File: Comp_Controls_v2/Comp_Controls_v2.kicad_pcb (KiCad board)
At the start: 2 copper layers, 78.1 x 108.9 mm, 42 parts

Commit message: fixed DRC warnings so far
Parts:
- removed ? (x3): , 
- renumbered VectorNavInput1 to VectorNavInput
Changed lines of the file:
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@@
 			(at -0.21 -1.05 0)
 			(layer "F.SilkS")
+			(hide yes)
 			(effects
 				(font
@@
 			(at -2.13 0.04 180)
 			(layer "F.SilkS")
+			(hide yes)
 			(effects
 				(font
@@
 			(at 1.54 1.05 90)
 			(layer "F.Fab")
+			(hide yes)
 			(effects
 				(font
@@
 		(descr "9-pin D-Sub connector, straight/vertical, THT-mount, socket (female), pitch 2.77x2.84mm, distance of mounting holes 25mm, see https://disti-assets.s3.amazonaws.com/tonar/files/datasheets/16730.pdf")
 		(tags "9-pin D-Sub connector straight vertical THT socket pitch 2.77x2.84mm mounting holes distance 25mm")
-		(property "Reference" "VectorNavInput1"
-			(at -5.54 -5.89 90)
+		(property "Reference" "VectorNavInput"
+			(at -6.17 9.38 90)
 			(layer "F.SilkS")
 			(effects
@@
 			(at -2.03 -0.09 180)
 			(layer "F.SilkS")
+			(hide yes)
 			(effects
 				(font
@@
 		(embedded_fonts no)
 	)
-	(footprint ""
-		(layer "F.Cu")
-		(at 118.915 39.48)
-		(property "Reference" ""
-			(at 0 0 0)
-			(layer "F.SilkS")
-			(effects
-				(font
-					(size 1.27 1.27)
-					(thickness 0.15)
-				)
-			)
-		)
-		(property "Value" ""
-			(at 0 0 0)
-			(layer "F.Fab")
-			(effects
-				(font
-					(size 1.27 1.27)
-					(thickness 0.15)
-				)
-			)
-		)
-		(property "Datasheet" ""
-			(at 0 0 0)
-			(layer "F.Fab")
-			(hide yes)
-			(effects
-				(font
-					(size 1.27 1.27)
-					(thickness 0.15)
-				)
-			)
-		)
-		(property "Description" ""
-			(at 0 0 0)
-			(layer "F.Fab")
-			(hide yes)
-			(effects
-				(font
-					(size 1.27 1.27)
-					(thickness 0.15)
-				)
-			)
-		)
-		(pad "" np_thru_hole circle
-			(at 0 0)
-			(size 3.2 3.2)
-			(drill 3.2)
-			(layers "*.Cu" "*.Mask")
-		)
-		(embedded_fonts no)
-	)
-	(footprint ""
-		(layer "F.Cu")
-		(at 188.115 39.47)
-		(property "Reference" ""
-			(at 0 0 0)
-			(layer "F.SilkS")
-			(effects
-				(font
-					(size 1.27 1.27)
-					(thickness 0.15)
-				)
-			)
-		)
-		(property "Value" ""
-			(at 0 0 0)
-			(layer "F.Fab")
-			(effects
-				(font
-					(size 1.27 1.27)
-					(thickness 0.15)
-				)
-			)
-		)
-		(property "Datasheet" ""
-			(at 0 0 0)
-			(layer "F.Fab")
-			(hide yes)
-			(effects
-				(font
-					(size 1.27 1.27)
-					(thickness 0.15)
-				)
-			)
-		)
-		(property "Description" ""
-			(at 0 0 0)
-			(layer "F.Fab")
-			(hide yes)
-			(effects
-				(font
-					(size 1.27 1.27)
-					(thickness 0.15)
-				)
-			)
-		)
-		(pad "" np_thru_hole circle
-			(at 0 0)
-			(size 3.2 3.2)
-			(drill 3.2)
-			(layers "*.Cu" "*.Mask")
-		)
-		(embedded_fonts no)
-	)
 	(footprint "Comp_Controls_v2:CAP_EEE1A_1000uf"
 		(layer "F.Cu")
@@
 		(embedded_fonts no)
 	)
-	(footprint ""
-		(layer "F.Cu")
-		(at 118.865 139.52)
-		(property "Reference" ""
-			(at 0 0 0)
-			(layer "F.SilkS")
-			(effects
-				(font
-					(size 1.27 1.27)
-					(thickness 0.15)
-				)
-			)
-		)
-		(property "Value" ""
-			(at 0 0 0)
-			(layer "F.Fab")
-			(effects
-				(font
-					(size 1.27 1.27)
-					(thickness 0.15)
-				)
-			)
-		)
-		(property "Datasheet" ""
-			(at 0 0 0)
-			(layer "F.Fab")
-			(hide yes)
-			(effects
-				(font
-					(size 1.27 1.27)
-					(thickness 0.15)
-				)
-			)
-		)
-		(property "Description" ""
-			(at 0 0 0)
-			(layer "F.Fab")
-			(hide yes)
-			(effects
-				(font
-					(size 1.27 1.27)
-					(thickness 0.15)
-				)
-			)
-		)
-		(pad "" np_thru_hole circle
-			(at 0 0)
-			(size 3.2 3.2)
-			(drill 3.2)
-			(layers "*.Cu" "*.Mask")
-		)
-		(embedded_fonts no)
-	)
 	(footprint "Connector_Molex:Molex_Mini-Fit_Jr_5566-06A_2x03_P4.20mm_Vertical"
 		(layer "F.Cu")
@@
 			(at 3 -0.05 180)
 			(layer "F.SilkS")
+			(hide yes)
 			(effects
 				(font
@@
 		(min_thickness 0.25)
 		(filled_areas_thickness no)
-		(fill yes
+		(fill
 			(thermal_gap 0.5)
 			(thermal_bridge_width 0.5)

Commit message: Add power traces
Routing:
- net +3.3V_SYS: track 0.00 -> 59.4 mm, vias 0 -> 2
- net +5V_SYS1: track 0.00 -> 55.5 mm, vias 0 -> 4
- net 16: track 0.00 -> 12.9 mm, vias 0 -> 2
- net Net-(VectorNavInput1-Pad7): track 0.00 -> 2.77 mm
- net XBeeTX: vias 6 -> 5

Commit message: Extra traces + power traces are done
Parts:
- moved 3.3V_MID1 2.37 mm to (173.7, 68.0)
- renumbered 3.3v_extra1 to 3.3V_EXTRA, 3.3v_LED to 3.3V_LED, 3.3V_SYS1 to 3.3V_SYS, 5v_extra1 to 5V_EXTRA, 5v_LED1 to 5V_LED, 5V_SYS1 to 5V_SYS, ANEMOMETER1 to ANEMOMETER, JIB1 to JIB, RUDDER1 to RUDDER, SAIL1 to SAIL, StepDownChip1 to StepDownChip, TEENSY1 to TEENSY
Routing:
- net +3.3V_SYS: track 59.4 -> 190.9 mm, vias 2 -> 4
- net +5V_SYS1: track 55.5 -> 148.0 mm, vias 4 -> 5
- net 20: track 0.00 -> 12.4 mm, vias 0 -> 2
- net +5V_SYS2: track 0.00 -> 8.40 mm
- net GND: track 121.0 -> 119.2 mm, vias 27 -> 26

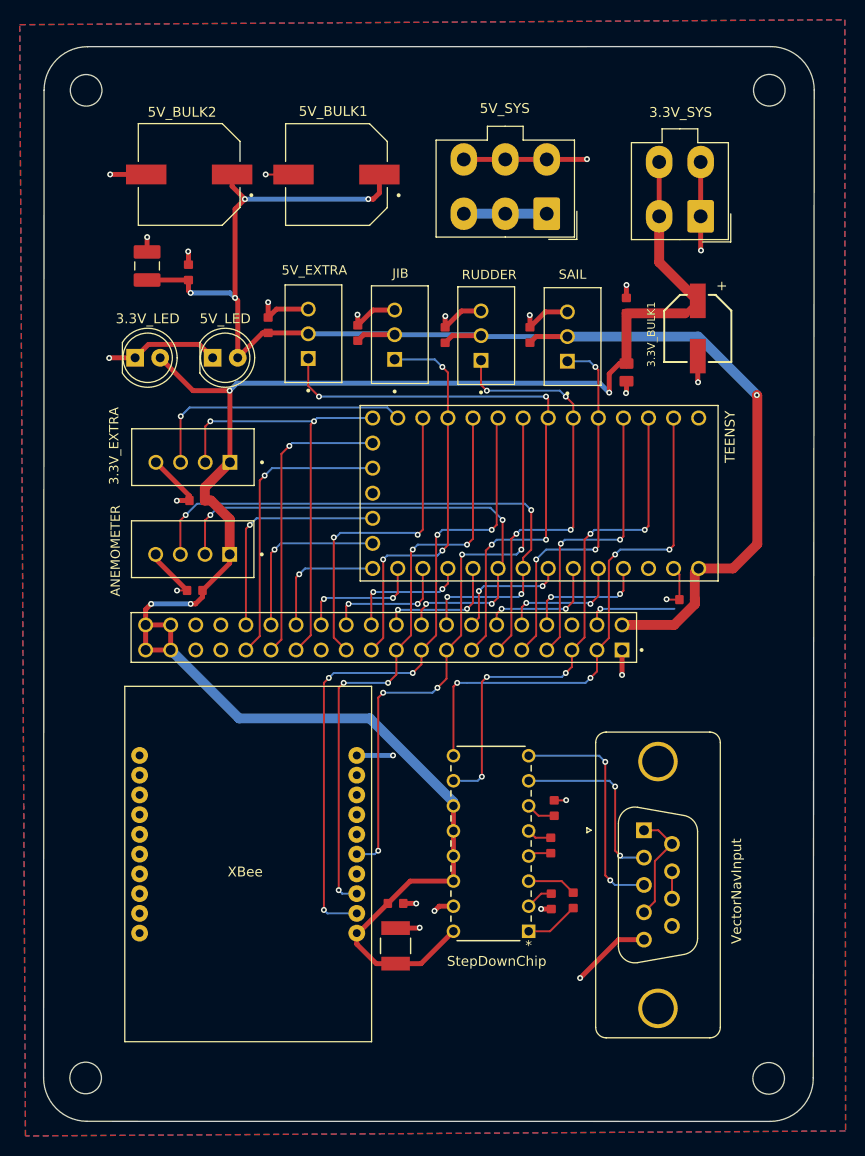
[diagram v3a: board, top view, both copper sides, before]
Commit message: silkscreen edits
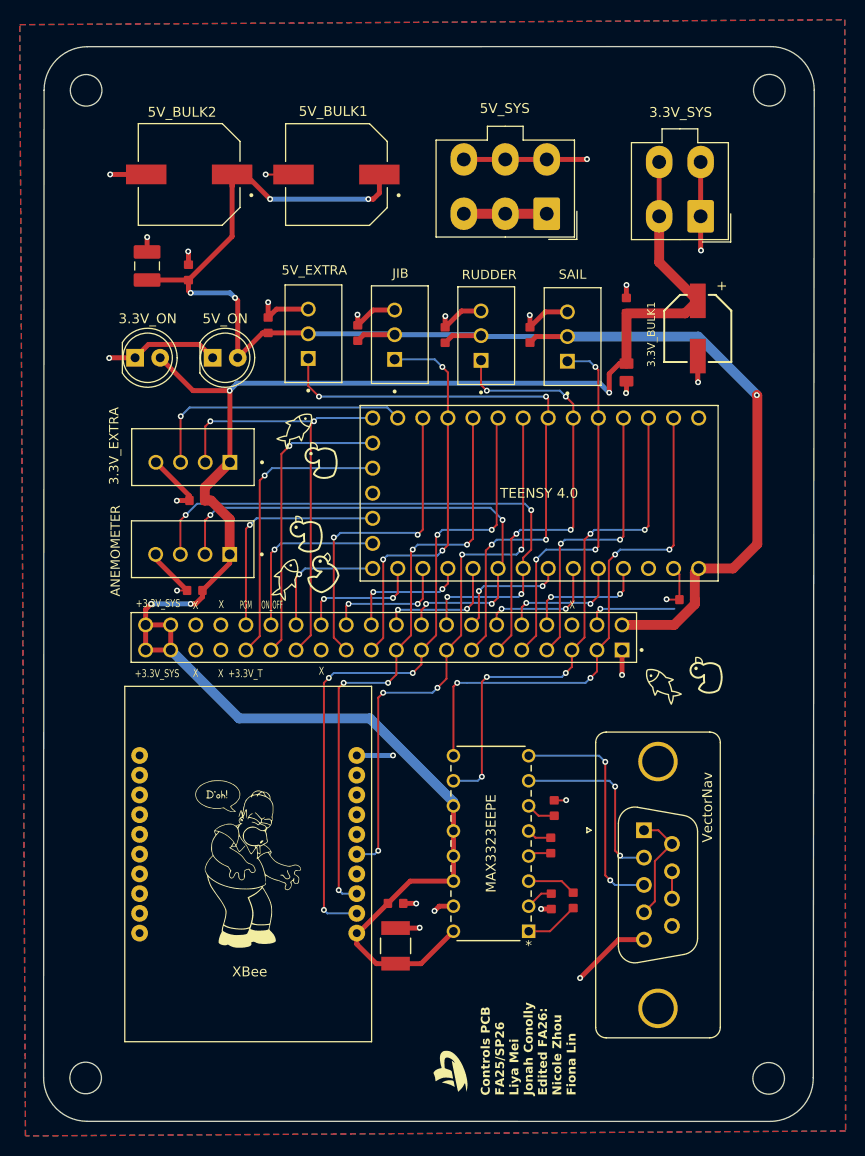
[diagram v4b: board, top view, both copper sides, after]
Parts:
- added G***: LOGO, LOGO, F.Cu at (181.7, 98.7)
- added G***: LOGO, LOGO, F.Cu at (177.2, 99.7)
- added G***: LOGO, LOGO, F.Cu at (142.7, 77.0)
- added G***: LOGO, LOGO, F.Cu at (142.9, 88.3)
- added G***: LOGO, LOGO, F.Cu at (140.2, 73.8)
- added G***: LOGO, LOGO, F.Cu at (141.2, 84.4)
- added G***: LOGO, LOGO, F.Cu at (135.4, 117.8)
- added G***: LOGO, LOGO, F.Cu at (139.2, 88.9)
- added G***: LOGO, LOGO, F.Cu at (155.8, 138.8)
- TEENSY 4.0: renamed from TEENSY
- renumbered 3.3V_LED to 3.3V_ON, 5V_LED to 5V_ON, StepDownChip to MAX3323EEPE, VectorNavInput to VectorNav
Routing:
- net +5V_SYS1: track 148.0 -> 150.6 mm
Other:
- board text added: "+3.3V_SYS"
- board text added: "+3.3V_T"
- board text added: "Controls PCB FA25/SP26 Liya Mei Jonah Conolly Edited FA26: Nicole Zhou Fiona Lin"
- board text added: "ON_OFF"
- board text added: "PGM"
- board text added: "X"
